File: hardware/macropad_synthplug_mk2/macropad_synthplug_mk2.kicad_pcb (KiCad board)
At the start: 2 copper layers, 59.6 x 36.1 mm, 38 parts, among them J1 Qwiic_RA, J2 AudioJack4, J3 AudioJack4, J4 AudioJack4, J5 Conn_01x04, SW1 K3-2346S-L1, SW2 K3-2346S-L1, U1 H11L1S(TA), U2 74HC14

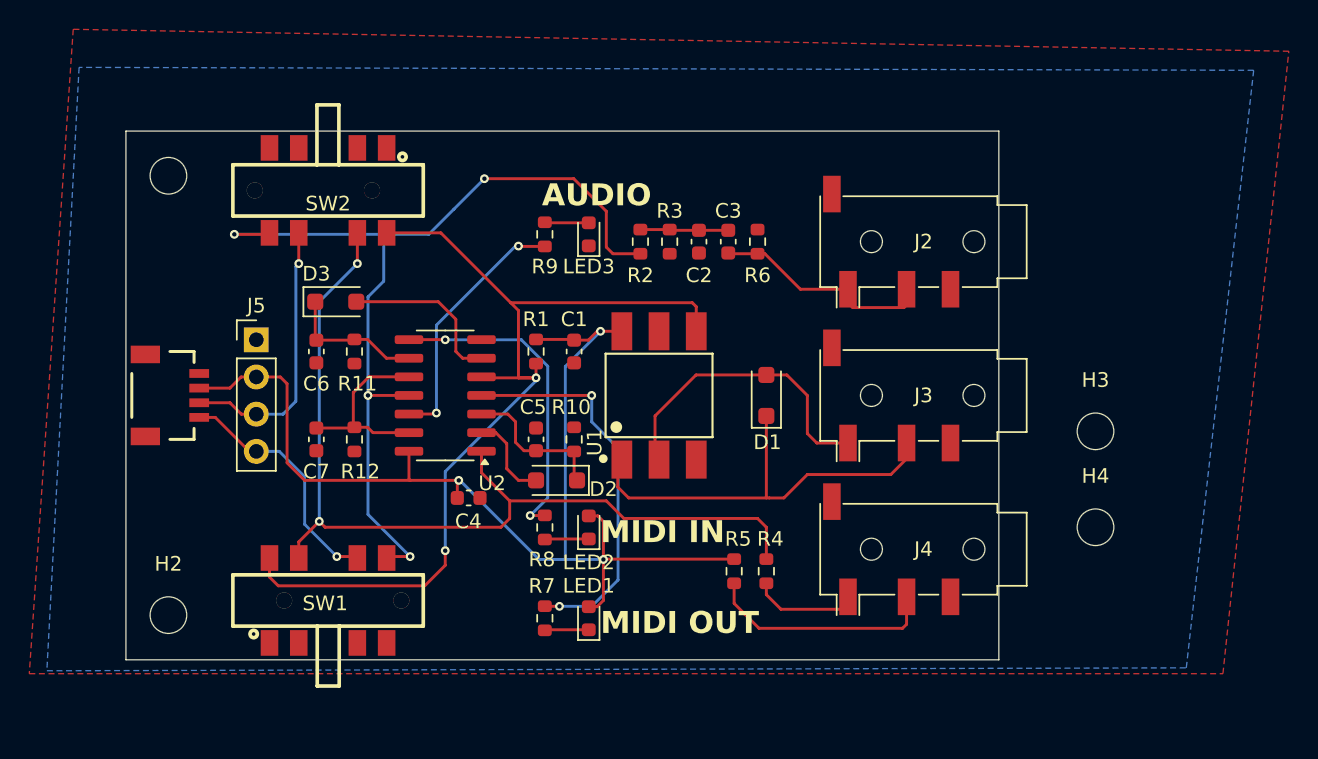
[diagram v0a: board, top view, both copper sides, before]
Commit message: mk2 size and silkscreen update
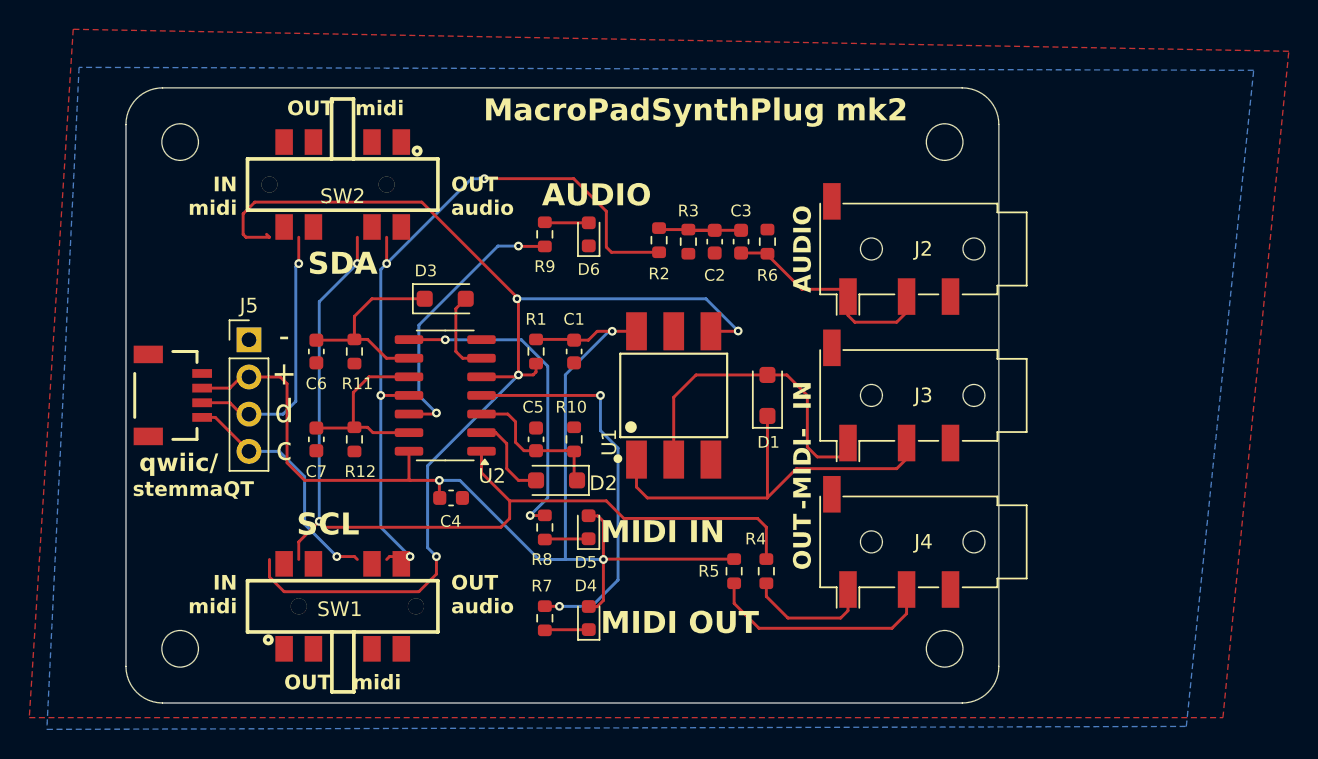
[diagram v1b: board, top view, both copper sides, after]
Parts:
- removed LED1, LED2, LED3: LED, LED_SMD:LED_0603_1608Metric
- added D4: LED, LED_SMD:LED_0603_1608Metric, F.Cu at (57.6, 59.2)
- added D5: LED, LED_SMD:LED_0603_1608Metric, F.Cu at (57.6, 53.0)
- added D6: LED, LED_SMD:LED_0603_1608Metric, F.Cu at (57.6, 33.0)
- moved H3 22.3 mm to (81.9, 26.7)
- moved H4 13.2 mm to (81.9, 61.3)
- moved D3 7.48 mm to (47.8, 37.4)
- moved H1 2.44 mm to (29.7, 26.7)
- moved H2 2.44 mm to (29.7, 61.3)
- moved R2 1.28 mm to (62.4, 33.4)
- moved R3 1.27 mm to (64.4, 33.5)
- moved C4 1.20 mm to (48.2, 51.0)
- moved SW1 1.08 mm to (40.8, 58.4)
- moved SW2 1.08 mm to (40.8, 29.6)
- moved C2 1.07 mm to (66.2, 33.5)
- moved U1 1.00 mm to (63.4, 44.0)
- moved C3 0.88 mm to (68.0, 33.5)
- moved R6 0.67 mm to (69.8, 33.5)
- moved J2 0.50 mm to (79.1, 34.0)
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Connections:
- SW2 pad 5: /PWM_AUDIO_OUT -> /MIDI_IN
- SW2 pad 8: /MIDI_IN -> /PWM_AUDIO_OUT
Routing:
- net /MIDI_IN: track 65.4 -> 83.0 mm, vias 2 -> 4
- net /PWM_AUDIO_OUT: track 63.6 -> 50.9 mm
- net Net-(D3-A): track 12.0 -> 6.35 mm
- net Net-(D3-K): track 9.99 -> 14.4 mm
- net Net-(J4-PadT): track 6.76 -> 8.74 mm
- net Net-(R9-Pad2): track 17.6 -> 19.2 mm
- net Net-(D1-A): track 20.8 -> 22.1 mm
- net Net-(D1-K): track 29.7 -> 28.4 mm
- net +3.3V: track 79.9 -> 81.1 mm
- net Net-(C2-Pad1): track 6.37 -> 7.01 mm
- net /SDA: track 18.9 -> 18.4 mm
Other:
- board size 59.6 x 36.1 mm -> 59.6 x 42 mm
- board text added: "- + d c"
- board text added: "-MIDI-"
- board text added: "IN"
- board text added: "IN midi"
- board text added: "MacroPadSynthPlug mk2"
- board text added: "OUT"
- board text added: "OUT audio"
- board text added: "OUT midi"
- board text added: "SCL"
- board text added: "SDA"
- board text added: "qwiic/"
- board text added: "stemmaQT"

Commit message: mk2 routing fixes
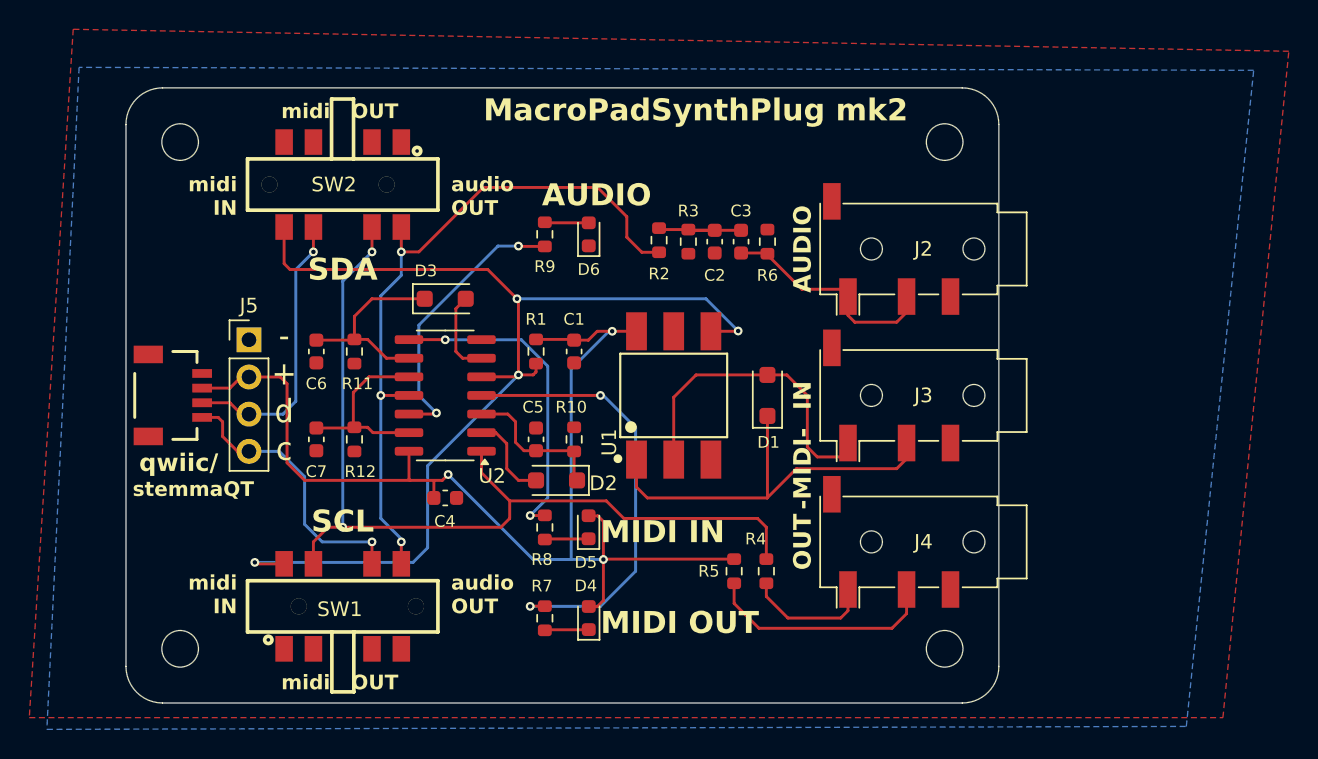
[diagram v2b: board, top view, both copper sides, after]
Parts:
- moved C4 0.40 mm to (47.8, 51.0)
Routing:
- net /MIDI_IN: track 83.0 -> 76.5 mm
- net Net-(R7-Pad2): track 27.0 -> 30.4 mm
- net /PWM_AUDIO_OUT: track 50.9 -> 48.2 mm, vias 4 -> 3
- net /SCL: track 16.5 -> 19.1 mm
- net /SDA: track 18.4 -> 19.5 mm
- net +3.3V: track 81.1 -> 81.7 mm
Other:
- board text added: "audio OUT"
- board text added: "midi IN"
- board text added: "midi OUT"
- board text removed: "IN midi"
- board text removed: "OUT audio"
- board text removed: "OUT midi"

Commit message: silkscreen for mk2
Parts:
- added G***: LOGO, LOGO, B.Cu at (65.0, 48.4)
- added G***: LOGO, LOGO, B.Cu at (43.0, 44.0)
- added kibuzzard-67216222: G***, kibuzzard-67216222, F.Cu at (40.8, 36.5)
- added kibuzzard-67216385: G***, kibuzzard-67216385, F.Cu at (40.8, 51.5)
- moved D6 4.29 mm to (57.6, 28.7)
- moved R9 4.29 mm to (54.6, 28.7)
- moved SW1 1.60 mm to (40.8, 60.0)
- moved SW2 1.60 mm to (40.8, 28.0)
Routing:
- net /MIDI_IN: track 76.5 -> 79.8 mm
- net /MIDI_OUT: track 62.7 -> 65.9 mm
- net Net-(R9-Pad2): track 19.2 -> 21.6 mm
- net /SDA: track 19.5 -> 21.1 mm
- net /PWM_AUDIO_OUT: track 48.2 -> 46.9 mm
- net /SCL: track 19.1 -> 20.2 mm
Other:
- board text added: "/ | \"
- board text added: "@todbot"
- board text added: "IN midi"
- board text added: "MacroPadSynthPlug mk2 @todbot - 25 Oct 2024 github.com/todbot/macropadsynthplug"
- board text added: "OUT audio"
- board text added: "OUT midi"
- board text added: "\ | /"
- board text added: "gnd 3v3 sda sdc"
- board text added: "– MIDI –"
- board text removed: "-MIDI-"

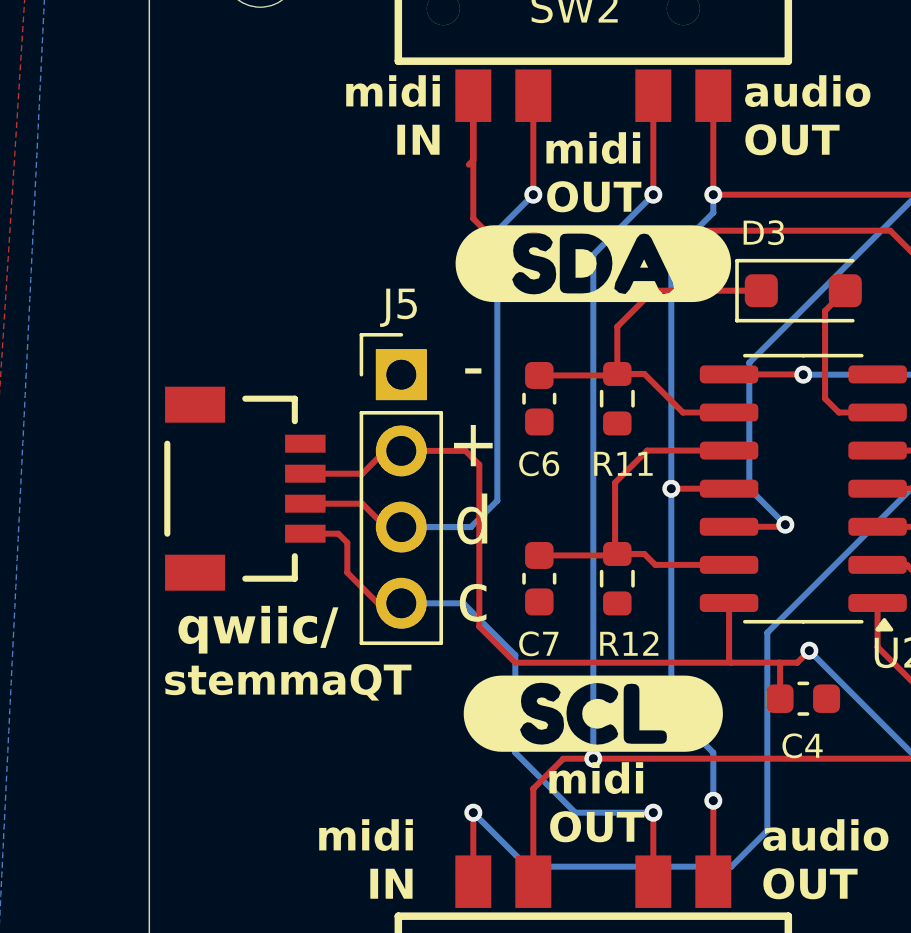
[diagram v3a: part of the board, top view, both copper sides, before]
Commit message: mk2 silkscreen update
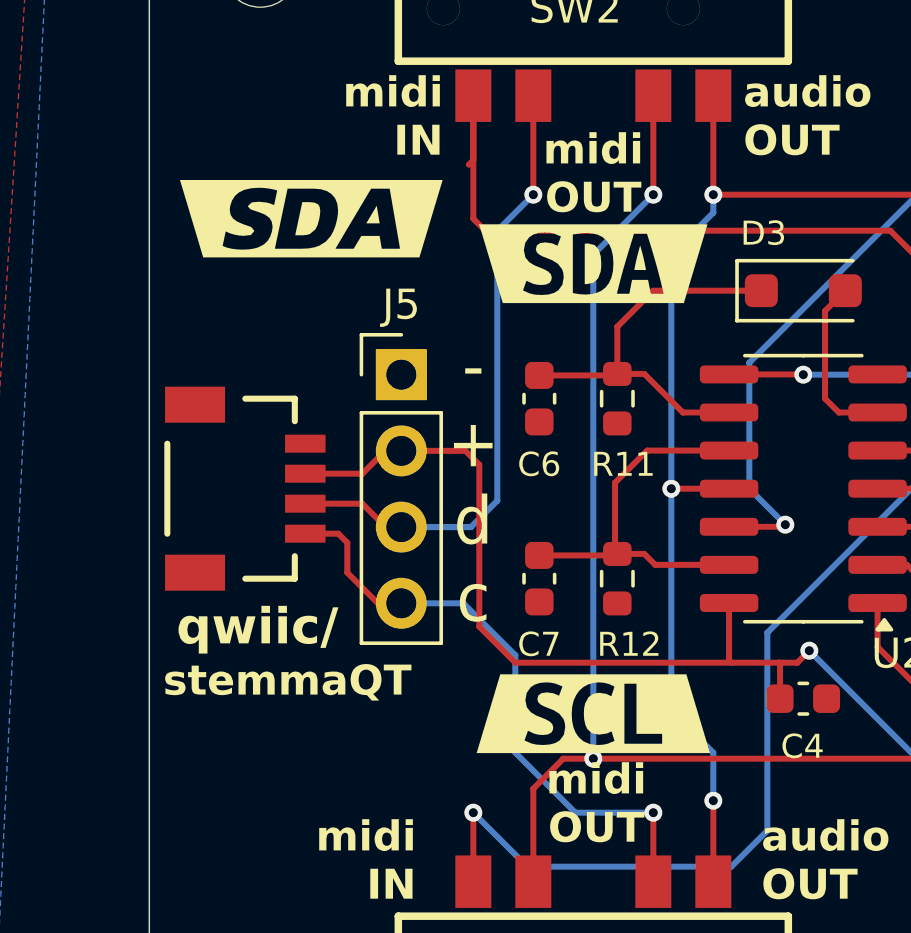
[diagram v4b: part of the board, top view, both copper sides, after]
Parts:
- removed kibuzzard-67216222: G***, kibuzzard-67216222
- removed kibuzzard-67216385: G***, kibuzzard-67216385
- added kibuzzard-6721CAF2: G***, kibuzzard-6721CAF2, F.Cu at (40.8, 36.5)
- added kibuzzard-6721CB0B: G***, kibuzzard-6721CB0B, F.Cu at (40.8, 51.5)
- added kibuzzard-6721CC38: G***, kibuzzard-6721CC38, F.Cu at (31.4, 35.0)
